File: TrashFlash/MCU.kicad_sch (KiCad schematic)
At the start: 0 parts

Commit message: Added STM32 to schematic
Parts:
- added C24, C25: 6.8p, symbol Device:C
- added IC11: STM32L471QEI6, BGA132C50P12X12_700X700X60, symbol TrashFlash:STM32L471QEI6
- added R40, R41, R42, R43: 1k, symbol Device:R
- added Y1: ECS-160-8-33B2-CTN-TR3, ECS160833B2CTNTR3, symbol TrashFlash:ECS-160-8-33B2-CTN-TR3
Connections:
- new net: C24.2, R40.2, Y1.3 (OUT/IN)
- new net: C25.1, IC11.G1 (PH1-_OSC_OUT), Y1.1 (IN/OUT)
- new net: IC11.F1 (PH0-OSC_IN), R40.1
- new net BOOT0: IC11.A4 (BOOT0), R42.2, R43.1
- new net GND: C24.1, C25.2, R42.1, Y1.2 (GND_1), Y1.4 (GND_2)
- new net NRST: IC11.H2 (NRST), R41.1
- new net VDD: R41.2, R43.2

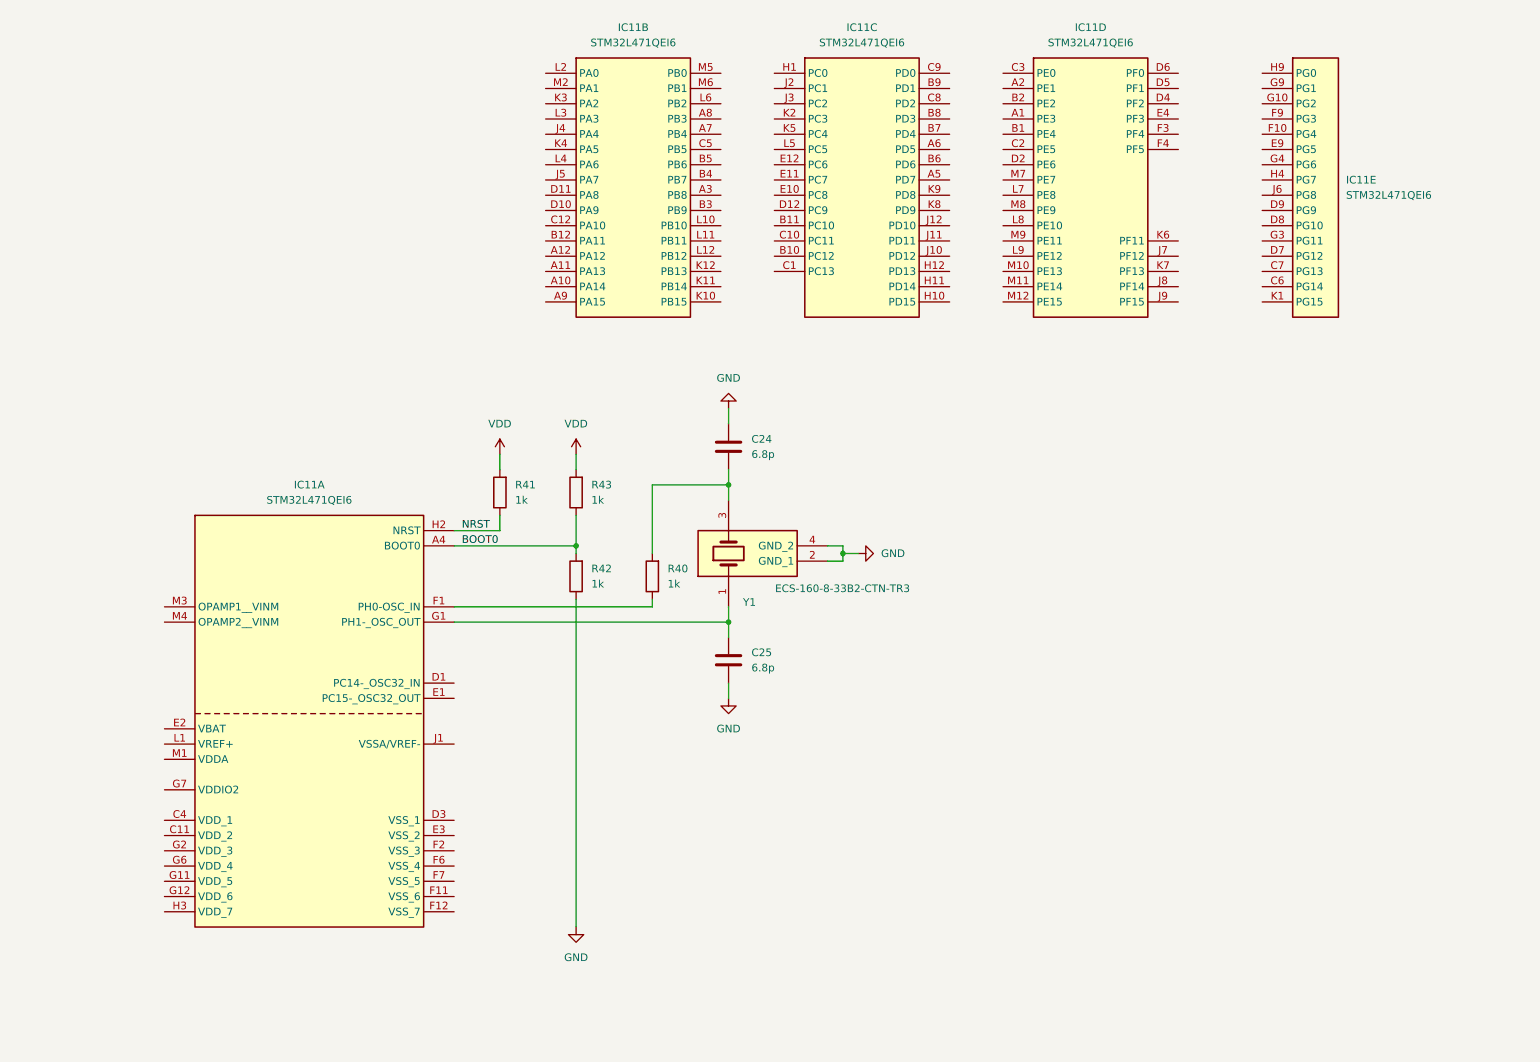
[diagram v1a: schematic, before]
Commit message: Added power supply to STM32
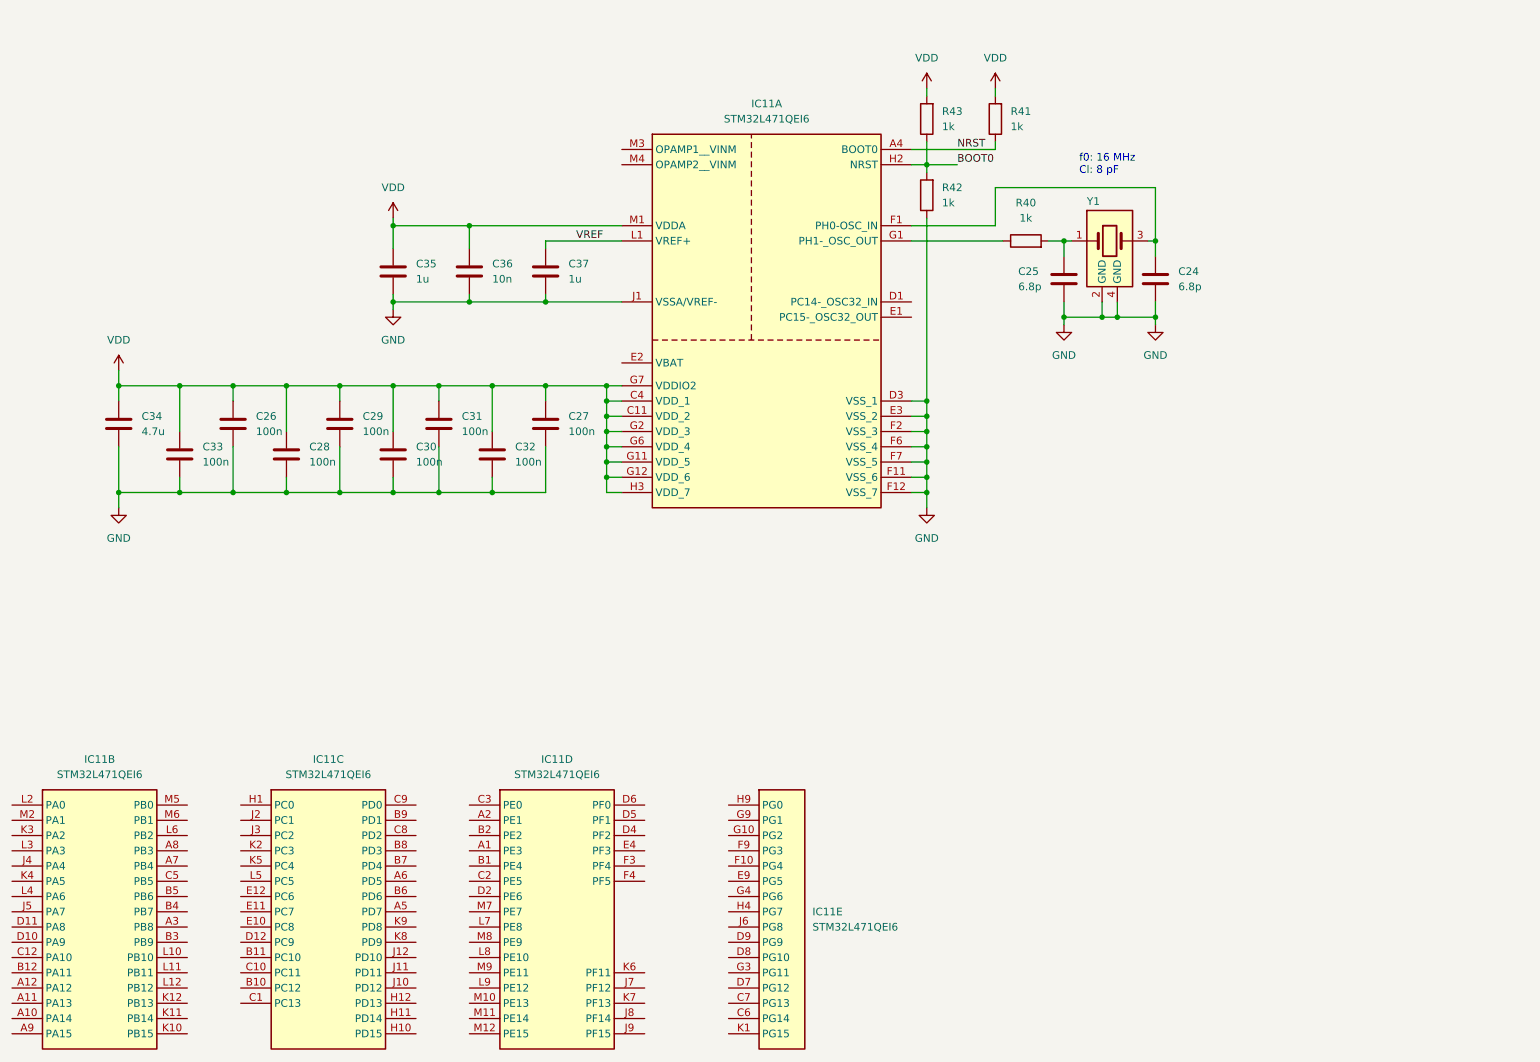
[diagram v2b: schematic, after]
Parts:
- added C26, C27, C28, C29, C30, C31, C32, C33: 100n, symbol Device:C
- added C34: 4.7u, symbol Device:C
- added C35, C37: 1u, symbol Device:C
- added C36: 10n, symbol Device:C
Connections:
- net BOOT0: now also IC11.H2 (NRST); no longer IC11.A4 (BOOT0)
- net GND: now also C24.2, IC11.D3 (VSS_1), IC11.E3 (VSS_2), IC11.F11 (VSS_6), IC11.F12 (VSS_7), IC11.F2 (VSS_3), IC11.F6 (VSS_4), IC11.F7 (VSS_5), IC11.J1 (VSSA/VREF-), C26.2, C27.2, C28.2, C29.2, C30.2, C31.2, C32.2, C33.2, C34.2, C35.2, C36.2, C37.2; no longer C24.1
- net NRST: now also IC11.A4 (BOOT0); no longer IC11.H2 (NRST)
- net VDD: now also IC11.C11 (VDD_2), IC11.C4 (VDD_1), IC11.G11 (VDD_5), IC11.G12 (VDD_6), IC11.G2 (VDD_3), IC11.G6 (VDD_4), IC11.G7 (VDDIO2), IC11.H3 (VDD_7), IC11.M1 (VDDA), C26.1, C27.1, C28.1, C29.1, C30.1, C31.1, C32.1, C33.1, C34.1, C35.1, C36.1
- net at C25.1, Y1.1 (IN/OUT): now also R40.2; no longer IC11.G1 (PH1-_OSC_OUT)
- net at R40.1: now also IC11.G1 (PH1-_OSC_OUT); no longer IC11.F1 (PH0-OSC_IN)
- net VREF: now reaches IC11.L1 (VREF+)
- net VREF: now also C37.1
- new net: C24.1, IC11.F1 (PH0-OSC_IN), Y1.3 (OUT/IN)
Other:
- note added: "f0: 16 MHz Cl: 8 pF"
- moved on the sheet: IC11B, IC11C, IC11D, IC11E, R41, R42, R43, Y1

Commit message: Changed the layout of MCU schematic
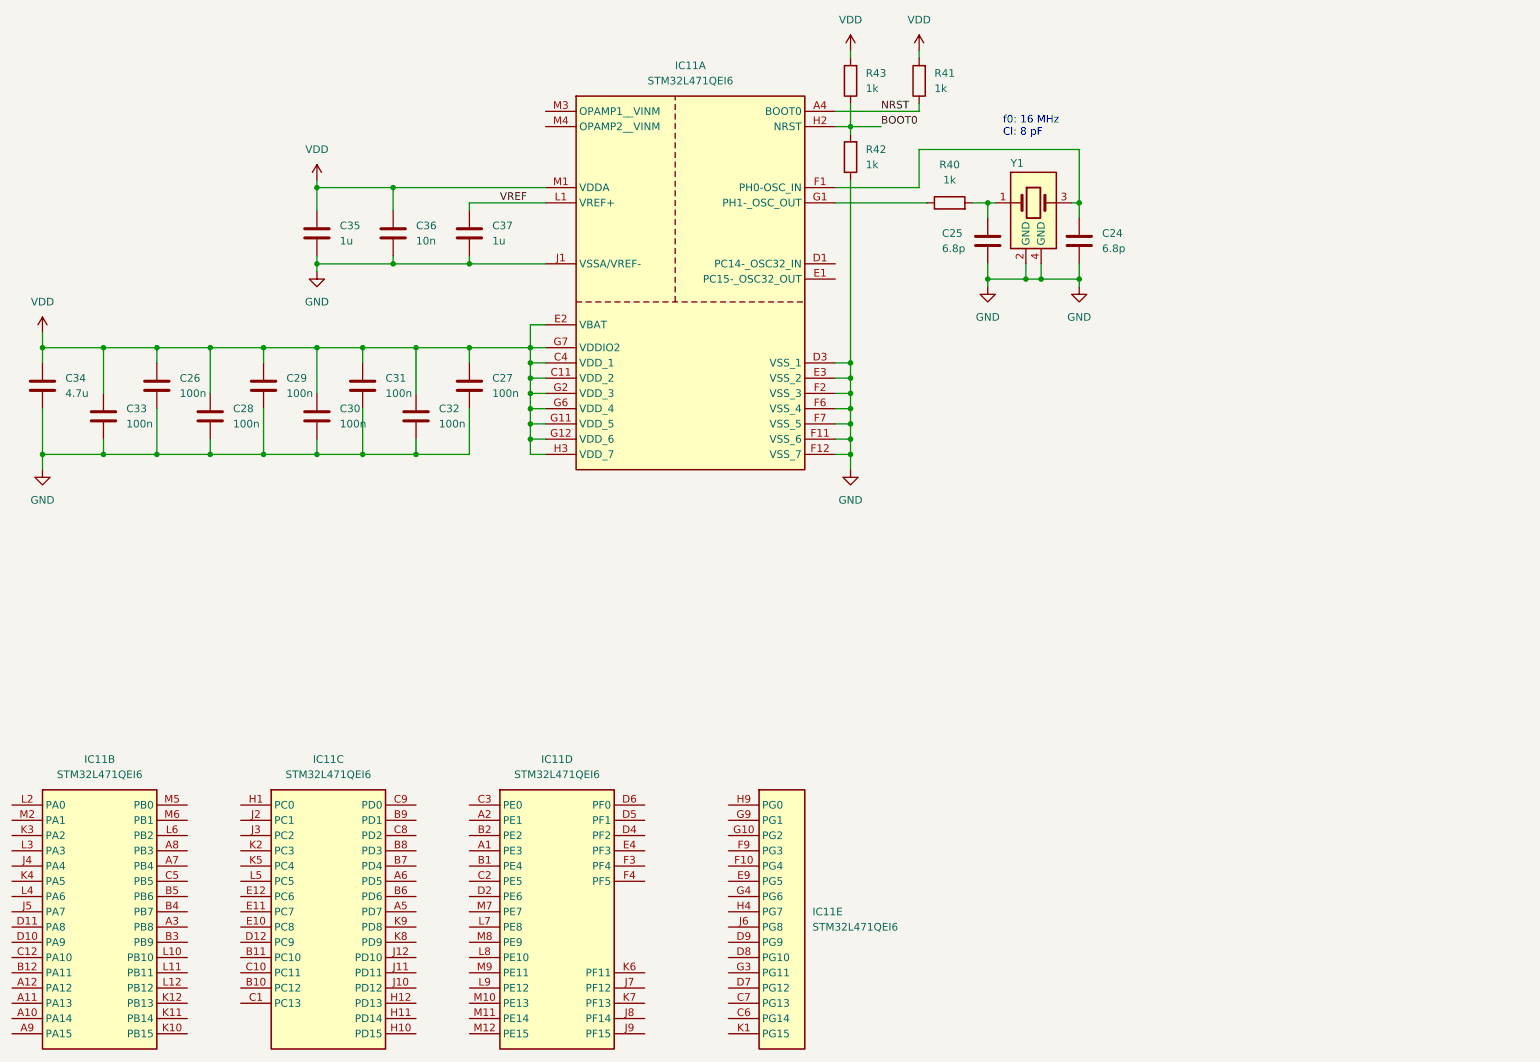
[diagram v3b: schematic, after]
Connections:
- net VDD: now also IC11.E2 (VBAT)
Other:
- moved on the sheet: C24, C25, C26, C27, C28, C29, C30, C31, C32, C33, C34, C35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

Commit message: Added 3D-models to footprints, PCB outline and component placement
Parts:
- C24, C25, C26, C27, C28, C29, C30, C31, C32, C33, C36: footprint (none) -> Capacitor_SMD:C_0402_1005Metric
- C34, C35, C37: footprint (none) -> Capacitor_SMD:C_0603_1608Metric
- IC11: footprint BGA132C50P12X12_700X700X60 -> TrashFlash:BGA132C50P12X12_700X700X60
- R40, R41, R42, R43: footprint (none) -> Resistor_SMD:R_0402_1005Metric
- Y1: footprint ECS160833B2CTNTR3 -> TrashFlash:ECS160833B2CTNTR3
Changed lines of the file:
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@@
 			)
 		)
-		(property "Footprint" ""
+		(property "Footprint" "Capacitor_SMD:C_0603_1608Metric"
 			(at 26.3652 83.82 0)
 			(effects
@@
 			)
 		)
-		(property "Footprint" ""
+		(property "Footprint" "Capacitor_SMD:C_0402_1005Metric"
 			(at 88.5952 88.9 0)
 			(effects
@@
 			)
 		)
-		(property "Footprint" ""
+		(property "Footprint" "Capacitor_SMD:C_0603_1608Metric"
 			(at 72.0852 58.42 0)
 			(effects
@@
 			)
 		)
-		(property "Footprint" ""
+		(property "Footprint" "Resistor_SMD:R_0402_1005Metric"
 			(at 176.53 51.308 90)
 			(effects
@@
 			)
 		)
-		(property "Footprint" ""
+		(property "Footprint" "Capacitor_SMD:C_0402_1005Metric"
 			(at 79.7052 83.82 0)
 			(effects
@@
 			)
 		)
-		(property "Footprint" "BGA132C50P12X12_700X700X60"
+		(property "Footprint" "TrashFlash:BGA132C50P12X12_700X700X60"
 			(at 25.4 124.46 0)
 			(effects
@@
 			)
 		)
-		(property "Footprint" ""
+		(property "Footprint" "Capacitor_SMD:C_0402_1005Metric"
 			(at 36.5252 88.9 0)
 			(effects
@@
 			)
 		)
-		(property "Footprint" "ECS160833B2CTNTR3"
+		(property "Footprint" "TrashFlash:ECS160833B2CTNTR3"
 			(at 186.69 77.47 0)
 			(effects
@@
 			)
 		)
-		(property "Footprint" "BGA132C50P12X12_700X700X60"
+		(property "Footprint" "TrashFlash:BGA132C50P12X12_700X700X60"
 			(at 144.78 124.46 0)
 			(effects
@@
 			)
 		)
-		(property "Footprint" "BGA132C50P12X12_700X700X60"
+		(property "Footprint" "TrashFlash:BGA132C50P12X12_700X700X60"
 			(at 101.6 124.46 0)
 			(effects
@@
 			)
 		)
-		(property "Footprint" "BGA132C50P12X12_700X700X60"
+		(property "Footprint" "TrashFlash:BGA132C50P12X12_700X700X60"
 			(at 63.5 124.46 0)
 			(effects
@@
 			)
 		)
-		(property "Footprint" ""
+		(property "Footprint" "Capacitor_SMD:C_0603_1608Metric"
 			(at 97.4852 58.42 0)
 			(effects
@@
 			)
 		)
-		(property "Footprint" ""
+		(property "Footprint" "Capacitor_SMD:C_0402_1005Metric"
 			(at 72.0852 88.9 0)
 			(effects
@@
 			)
 		)
-		(property "Footprint" ""
+		(property "Footprint" "Capacitor_SMD:C_0402_1005Metric"
 			(at 183.8452 59.69 0)
 			(effects
@@
 			)
 		)
-		(property "Footprint" ""
+		(property "Footprint" "Resistor_SMD:R_0402_1005Metric"
 			(at 173.228 29.21 90)
 			(effects
@@
 			)
 		)
-		(property "Footprint" ""
+		(property "Footprint" "Resistor_SMD:R_0402_1005Metric"
 			(at 161.798 29.21 90)
 			(effects
@@
 			)
 		)
-		(property "Footprint" ""
+		(property "Footprint" "Capacitor_SMD:C_0402_1005Metric"
 			(at 199.0852 59.69 0)
 			(effects
@@
 			)
 		)
-		(property "Footprint" ""
+		(property "Footprint" "Resistor_SMD:R_0402_1005Metric"
 			(at 161.798 41.91 90)
 			(effects
@@
 			)
 		)
-		(property "Footprint" "BGA132C50P12X12_700X700X60"
+		(property "Footprint" "TrashFlash:BGA132C50P12X12_700X700X60"
 			(at 114.3 8.89 0)
 			(effects
@@
 			)
 		)
-		(property "Footprint" ""
+		(property "Footprint" "Capacitor_SMD:C_0402_1005Metric"
 			(at 54.3052 88.9 0)
 			(effects
@@
 			)
 		)
-		(property "Footprint" ""
+		(property "Footprint" "Capacitor_SMD:C_0402_1005Metric"
 			(at 84.7852 58.42 0)
 			(effects
@@
 			)
 		)
-		(property "Footprint" ""
+		(property "Footprint" "Capacitor_SMD:C_0402_1005Metric"
 			(at 63.1952 83.82 0)
 			(effects
@@
 			)
 		)
-		(property "Footprint" ""
+		(property "Footprint" "Capacitor_SMD:C_0402_1005Metric"
 			(at 97.4852 83.82 0)
 			(effects
@@
 			)
 		)
-		(property "Footprint" ""
+		(property "Footprint" "Capacitor_SMD:C_0402_1005Metric"
 			(at 45.4152 83.82 0)
 			(effects

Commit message: Added Wireless and inter PCB connector
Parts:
- IC401: renamed from IC11; footprint TrashFlash:BGA132C50P12X12_700X700X60 -> BGA132C50P12X12_700X700X60
- Y401: renamed from Y1; footprint TrashFlash:ECS160833B2CTNTR3 -> ECS160833B2CTNTR3
- renumbered C35 to C401, C36 to C402, C37 to C403, C25 to C404, C24 to C405, C34 to C406, C26 to C407, C29 to C408, C31 to C409, C27 to C410, C33 to C411, C28 to C412, C30 to C413, C32 to C414, R43 to R401, R41 to R402, R42 to R403, R40 to R404
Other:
- moved on the sheet: C401, C402, C407, C408, C411, C412, C413

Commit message: Moved USB and added JTAG connector
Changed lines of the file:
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@@
+		)
+	)
+	(hierarchical_label "T_JTDO{slash}T_SWO"
+		(shape output)
+		(at 232.41 143.51 0)
+		(effects
+			(font
+				(size 1.27 1.27)
+			)
+			(justify left)
 		)
 	)
@@
 		(shape output)
 		(at 232.41 36.83 0)
+		(effects
+			(font
+				(size 1.27 1.27)
+			)
+			(justify left)
+		)
+	)
+	(hierarchical_label "T_VCP_RX"
+		(shape input)
+		(at 232.41 151.13 0)
 		(effects
 			(font
@@
 		)
 	)
+	(hierarchical_label "T_JCLK{slash}T_SWCLK"
+		(shape input)
+		(at 232.41 140.97 0)
+		(effects
+			(font
+				(size 1.27 1.27)
+			)
+			(justify left)
+		)
+	)
 	(hierarchical_label "CSN"
 		(shape output)
@@
 		)
 	)
+	(hierarchical_label "T_NRST"
+		(shape input)
+		(at 232.41 148.59 0)
+		(effects
+			(font
+				(size 1.27 1.27)
+			)
+			(justify left)
+		)
+	)
+	(hierarchical_label "T_JTDI{slash}NC"
+		(shape input)
+		(at 232.41 146.05 0)
+		(fields_autoplaced yes)
+		(effects
+			(font
+				(size 1.27 1.27)
+			)
+			(justify left)
+		)
+		(property "Netclass" ""
+			(at 232.41 147.32 0)
+			(effects
+				(font
+					(size 1.27 1.27)
+					(italic yes)
+				)
+				(justify left)
+			)
+		)
+	)
 	(hierarchical_label "SELECT_VDD"
 		(shape output)
@@
 		)
 	)
+	(hierarchical_label "T_VCP_TX"
+		(shape output)
+		(at 232.41 153.67 0)
+		(effects
+			(font
+				(size 1.27 1.27)
+			)
+			(justify left)
+		)
+	)
 	(hierarchical_label "VMEAS_VDRIVE"
 		(shape input)
@@
 		(effects
 			(font
+				(size 1.27 1.27)
+			)
+			(justify left)
+		)
+	)
+	(hierarchical_label "T_JTMS{slash}T_SWDIO"
+		(shape bidirectional)
+		(at 232.41 138.43 0)
+		(effects
+			(font

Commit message: Added battery and connectors, Schematic remark for BQ297xx
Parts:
- IC401: footprint BGA132C50P12X12_700X700X60 -> TrashFlash:BGA132C50P12X12_700X700X60
- Y401: footprint ECS160833B2CTNTR3 -> TrashFlash:ECS160833B2CTNTR3
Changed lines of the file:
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@@
 			)
 		)
-		(property "Footprint" "BGA132C50P12X12_700X700X60"
+		(property "Footprint" "TrashFlash:BGA132C50P12X12_700X700X60"
 			(at 25.4 124.46 0)
 			(effects
@@
 			)
 		)
-		(property "Footprint" "ECS160833B2CTNTR3"
+		(property "Footprint" "TrashFlash:ECS160833B2CTNTR3"
 			(at 186.69 77.47 0)
 			(effects
@@
 			)
 		)
-		(property "Footprint" "BGA132C50P12X12_700X700X60"
+		(property "Footprint" "TrashFlash:BGA132C50P12X12_700X700X60"
 			(at 144.78 124.46 0)
 			(effects
@@
 			)
 		)
-		(property "Footprint" "BGA132C50P12X12_700X700X60"
+		(property "Footprint" "TrashFlash:BGA132C50P12X12_700X700X60"
 			(at 101.6 124.46 0)
 			(effects
@@
 			)
 		)
-		(property "Footprint" "BGA132C50P12X12_700X700X60"
+		(property "Footprint" "TrashFlash:BGA132C50P12X12_700X700X60"
 			(at 63.5 124.46 0)
 			(effects
@@
 			)
 		)
-		(property "Footprint" "BGA132C50P12X12_700X700X60"
+		(property "Footprint" "TrashFlash:BGA132C50P12X12_700X700X60"
 			(at 114.3 8.89 0)
 			(effects
